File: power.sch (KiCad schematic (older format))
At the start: 76 parts, among them J6 7-17 V IN, Q1 DMP3099L-7, SW7 JS202011SCQN, U1 ICE40HX4K-TQ144, U10 MAX40200AUK, U12 TPS562201, U15 MAX40200AUK, U21 MAX40200AUK, U6 TLV62568APDRLR, U7 TLV62568APDRLR

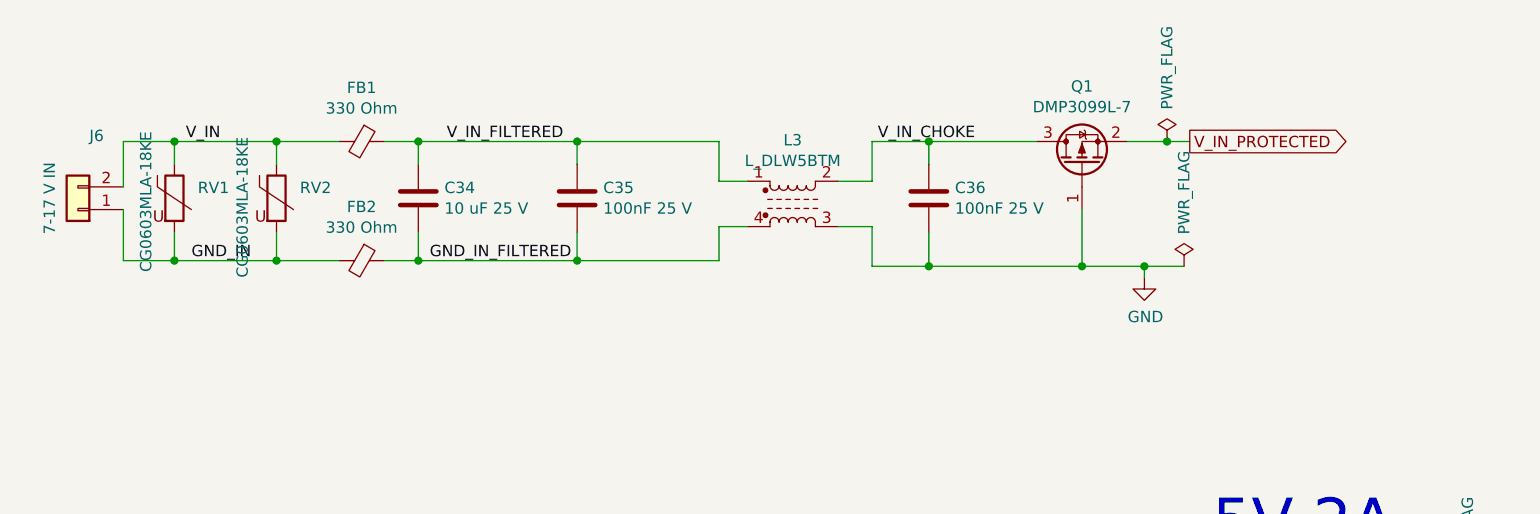
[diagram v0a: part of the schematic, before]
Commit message: 7-17VIN Power
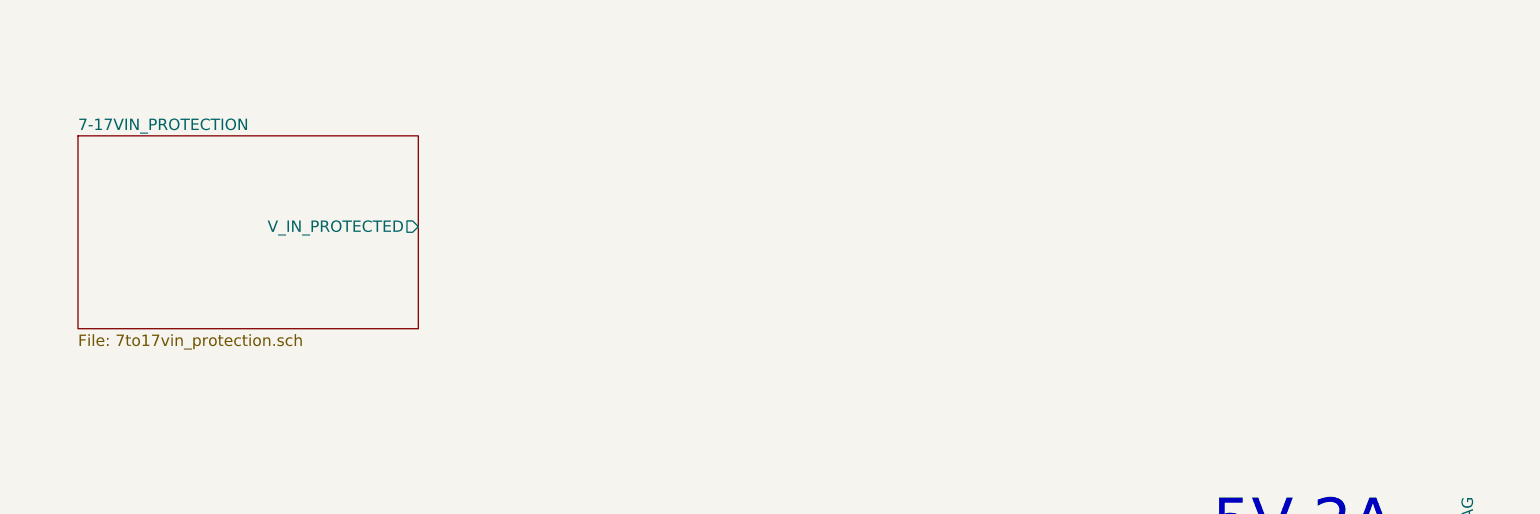
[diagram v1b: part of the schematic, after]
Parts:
- removed C34: 10 uF 25 V, Capacitor_SMD:C_0805_2012Metric, symbol Device:C
- removed C35, C36: 100nF 25 V, Capacitor_SMD:C_0603_1608Metric, symbol Device:C
- removed FB1, FB2: 330 Ohm, Resistor_SMD:R_0805_2012Metric, symbol Device:Ferrite_Bead_Small
- removed J6: 7-17 V IN, TerminalBlock:TerminalBlock_bornier-2_P5.08mm, symbol Connector_Generic:Conn_01x02
- removed L3: L_DLW5BTM, footprints:L_Murata_DLW5BTM_5.00x5.00mm_footprint, symbol l_dlw5btm:L_DLW5BTM
- removed Q1: DMP3099L-7, Package_TO_SOT_SMD:SOT-23, symbol Device:Q_PMOS_GSD
- removed RV1, RV2: CG0603MLA-18KE, Resistor_SMD:R_0603_1608Metric, symbol Device:Varistor

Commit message: Voltage Regulators
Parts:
- removed C1, C3, C4, C5, C7, C8, C89: 10 uF 6,3 V, Capacitor_SMD:C_0603_1608Metric, symbol Device:C
- removed C2, C49, C6: 10pF 6,3 V, Capacitor_SMD:C_0603_1608Metric, symbol Device:C
- removed C37, C38: 10 uF 25 V, Capacitor_SMD:C_0805_2012Metric, symbol Device:C
- removed C41: 100nF 25 V, Capacitor_SMD:C_0603_1608Metric, symbol Device:C
- removed C43: 100nF 6,3 V, Capacitor_SMD:C_0603_1608Metric, symbol Device:C
- removed C44, C48: 22 uF 6,3 V, Capacitor_SMD:C_0603_1608Metric, symbol Device:C
- removed D9: LED_ALT, LED_SMD:LED_0603_1608Metric, symbol Device:LED_ALT
- removed L1, L2: 1u, footprints:L_1008_2520Metric_2.5x2mm_footprint, symbol Device:L
- removed L4: 4,7 uH, Inductor_SMD:L_Taiyo-Yuden_NR-50xx, symbol Device:L
- removed R14, R15: 100k 1%, Resistor_SMD:R_0603_1608Metric, symbol Device:R
- removed R16: 220k 1%, Resistor_SMD:R_0603_1608Metric, symbol Device:R
- removed R17: 48,7k 1%, Resistor_SMD:R_0603_1608Metric, symbol Device:R
- removed R18: 10k, Resistor_SMD:R_0603_1608Metric, symbol Device:R
- removed R19: 560, Resistor_SMD:R_0603_1608Metric, symbol Device:R
- removed R30: 0, Resistor_SMD:R_0805_2012Metric, symbol Device:R
- removed R35: 54k9 1%, Resistor_SMD:R_0603_1608Metric, symbol Device:R
- removed R40: 10k 1%, Resistor_SMD:R_0603_1608Metric, symbol Device:R
- removed U12: TPS562201, Package_TO_SOT_SMD:SOT-23-6, symbol Regulator_Switching:TPS562200
- removed U15, U21: MAX40200AUK, Package_TO_SOT_SMD:SOT-23-5, symbol Analog_Switch:MAX40200AUK
- removed U6, U7: TLV62568APDRLR, footprints:Texas_DRL_SOT-563_1.6x1.6mm_0.5mm-pitch_footprint, symbol TLV62568APDRLR:TLV62568APDRLR
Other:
- note removed: "1,2 V 1 A"
- note removed: "3,3 V 1 A"
- note removed: "5V 2A"
- note removed: "In case of noise in the 1.2 V net,\nreplace this resistor R30 with an inductor\nor an ferrite bead"
- note removed: "Note: Use TLV62568ADRLR for 2 A"
- moved on the sheet: D16, JP1, R48, R67, U10

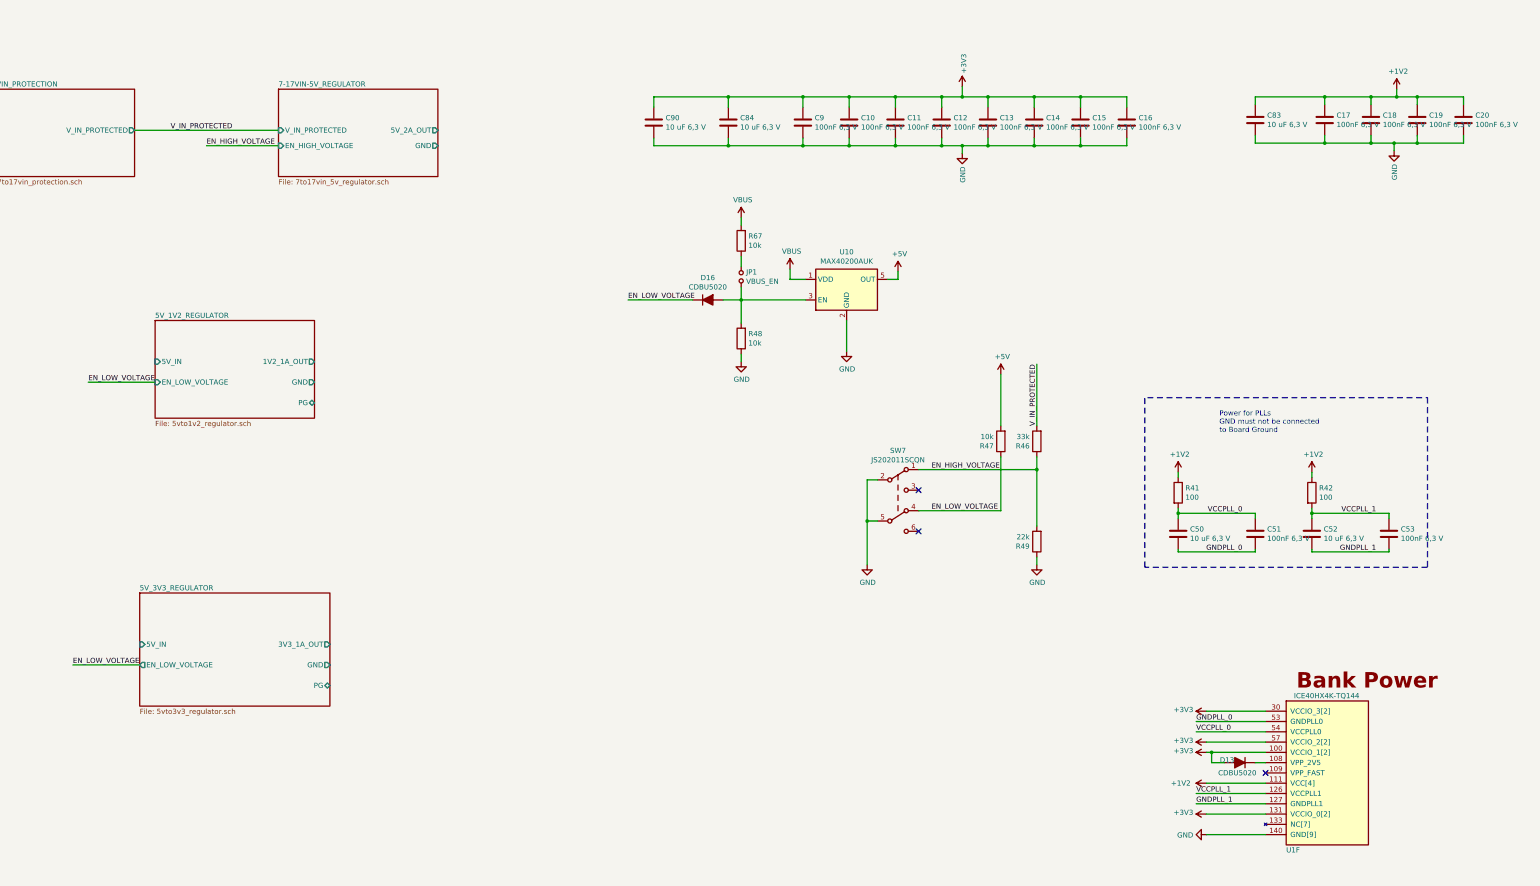
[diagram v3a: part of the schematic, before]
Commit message: Schematic modified (Hierarchy) Bug where SPI was active when creset or ss was low fixed PCB layout started (almost all parts are at position) No parts on the bottom so far Arduino and PMOD header spacings corrected according to its standards
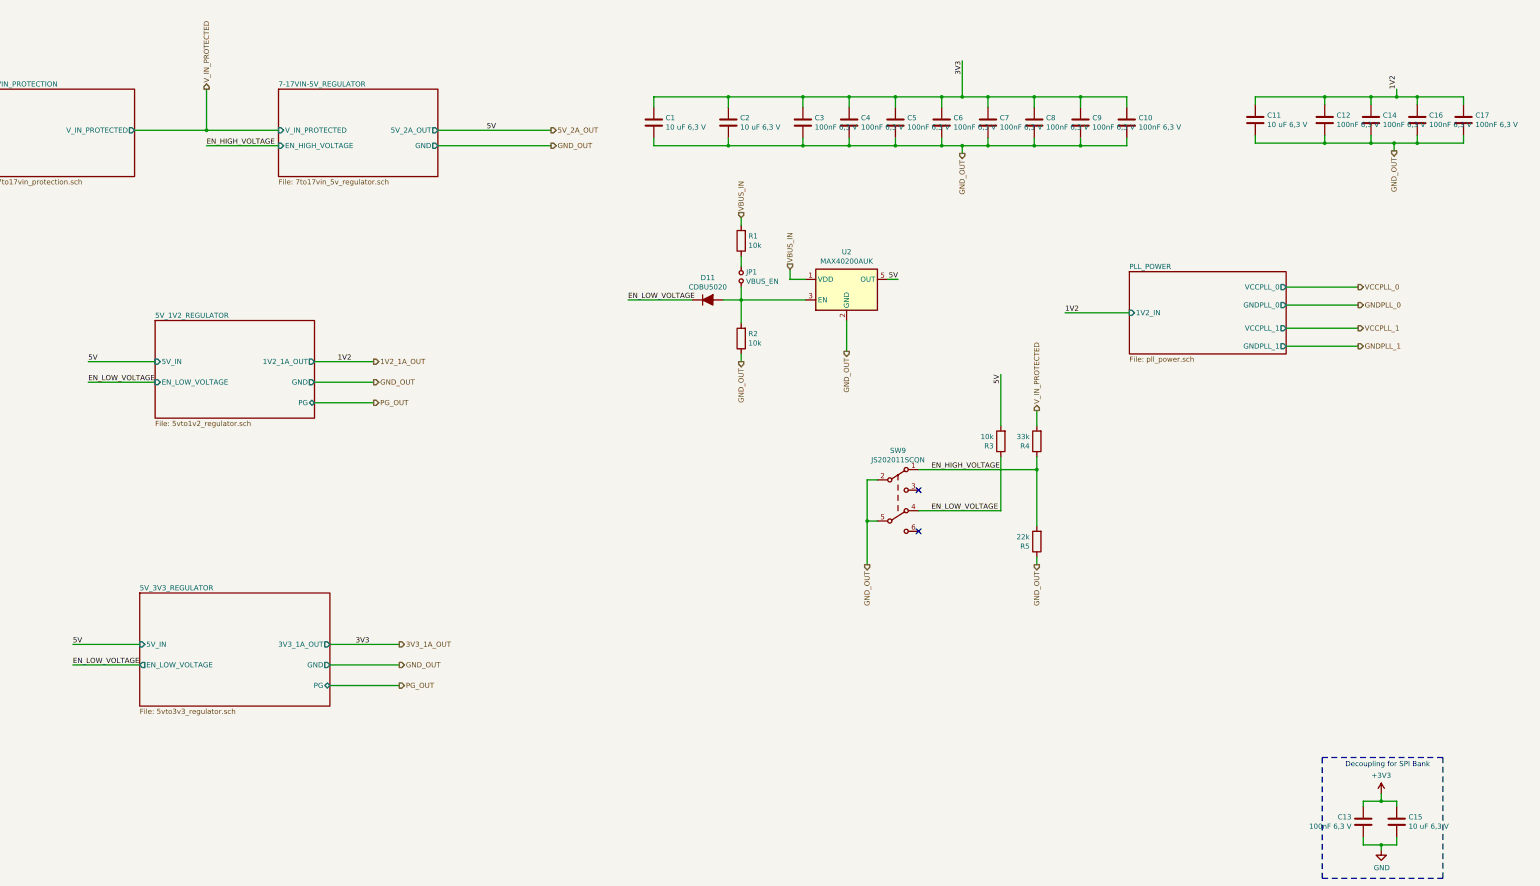
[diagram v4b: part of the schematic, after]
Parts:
- removed C50, C52: 10 uF 6,3 V, Capacitor_SMD:C_0603_1608Metric, symbol Device:C
- removed C51, C53: 100nF 6,3 V, Capacitor_SMD:C_0603_1608Metric, symbol Device:C
- removed D13: CDBU5020, Diode_SMD:D_0603_1608Metric, symbol Device:D_ALT
- removed R41, R42: 100, Resistor_SMD:R_0603_1608Metric, symbol Device:R
- removed U1: ICE40HX4K-TQ144, symbol ice40hx4k:ICE40HX4K-TQ144
- added C13: 100nF 6,3 V, Capacitor_SMD:C_0603_1608Metric, symbol Device:C
- added C15: 10 uF 6,3 V, Capacitor_SMD:C_0603_1608Metric, symbol Device:C
- renumbered C90 to C1, C16 to C10, C83 to C11, C17 to C12, C18 to C14, C19 to C16, C20 to C17, C84 to C2, C9 to C3, C10 to C4, C11 to C5, C12 to C6, C13 to C7, C14 to C8, C15 to C9, D16 to D11, R67 to R1, R48 to R2, R47 to R3, R46 to R4, R49 to R5, SW7 to SW9, U10 to U2
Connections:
- net +3V3: now also C13.1, C15.1; no longer C1.1, C10.1, C2.1, C3.1, C4.1, C5.1, C6.1, C7.1, C8.1, C9.1
- net GND: now also C13.2, C15.2; no longer C1.2, C10.2, C11.2, C12.2, C14.2, C16.2, C17.2, C2.2, C3.2, C4.2, C5.2, C6.2, C7.2, C8.2, C9.2, R2.1, R5.1, SW9.2 (B), SW9.5 (B), U2.2 (GND)
- net +1V2 renamed 1V2_1A_OUT
- net +5V renamed 5V_2A_OUT
- net VBUS renamed VBUS_IN
- new net 3V3_1A_OUT: C1.1, C10.1, C2.1, C3.1, C4.1, C5.1, C6.1, C7.1, C8.1, C9.1
- new net GND_OUT: C1.2, C10.2, C11.2, C12.2, C14.2, C16.2, C17.2, C2.2, C3.2, C4.2, C5.2, C6.2, C7.2, C8.2, C9.2, R2.1, R5.1, SW9.2 (B), SW9.5 (B), U2.2 (GND)
- no-connect marks 3 -> 2
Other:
- note added: "Decoupling for SPI Bank"
- note removed: "Power for PLLs\nGND must not be connected\nto Board Ground"

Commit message: Part specifications added to the VBUS Enable Jumper
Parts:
- JP1: Description (none) -> CONN HEADER VERT 2POS 2.54MM; Digikey (none) -> S1011EC-02-ND; Mfg Name (none) -> Sullins Connector Solutions; Mfg Part Num (none) -> PRPC002SAAN-RC; Spec (none) -> Any
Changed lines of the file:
@@
 F 2 "Connector_PinHeader_2.54mm:PinHeader_1x02_P2.54mm_Vertical" H 8350 3025 50  0001 C CNN
 F 3 "~" H 8350 3025 50  0001 C CNN
+F 4 "CONN HEADER VERT 2POS 2.54MM" H 8350 3025 50  0001 C CNN "Description"
+F 5 "S1011EC-02-ND" H 8350 3025 50  0001 C CNN "Digikey"
+F 6 "Sullins Connector Solutions" H 8350 3025 50  0001 C CNN "Mfg Name"
+F 7 "PRPC002SAAN-RC" H 8350 3025 50  0001 C CNN "Mfg Part Num"
+F 8 "Any" H 8350 3025 50  0001 C CNN "Spec"
 	1    8350 3025
 	0    1    1    0
